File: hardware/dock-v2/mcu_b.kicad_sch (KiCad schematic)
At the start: 31 parts, among them SW401 SW_Push, U401 RP2354A, Y401 12MHz

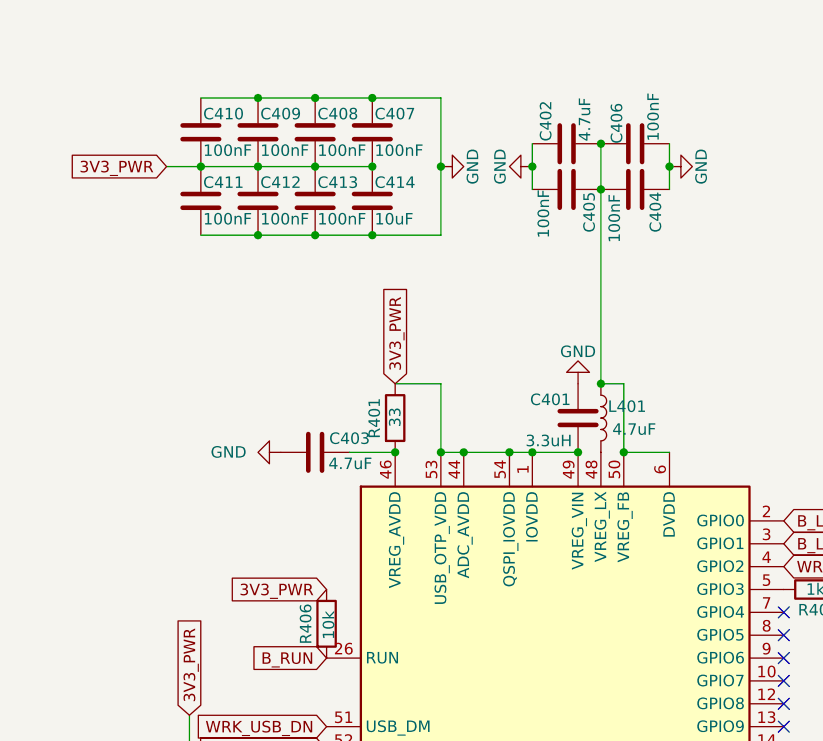
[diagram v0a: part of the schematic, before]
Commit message: Dock v2 schematic: PWR_FLAGs, one name per power net, ESP32 USB test pads dropped
- PWR_FLAGs on GND, VBUS_IN, 5V_PWR, A_1V1, A_VREG_AVDD, B_1V1, B_VREG_AVDD
  (each with a label at a pin of the net, which also names the five nets that
  were unnamed: VBUS_IN, A/B_1V1, A/B_VREG_AVDD)
- GNDPWR symbol -> GND; duplicate +3.3V/+5V power symbols and their now-dangling
  3V3_PWR/5V_PWR labels removed (connectivity verified identical before/after)
- TP501/TP502 (ESP32 GPIO18/19 USB pads) not needed: pins 26/27 are no-connects
  in the model; docs and guides updated (fallback flashing: TXD0/RXD0 pads)

ERC: 0 errors, 0 warnings. check_wiring.py: OK, wiring matches the guide.

Co-Authored-By: Claude Opus 5.5 <noreply@anthropic.com>
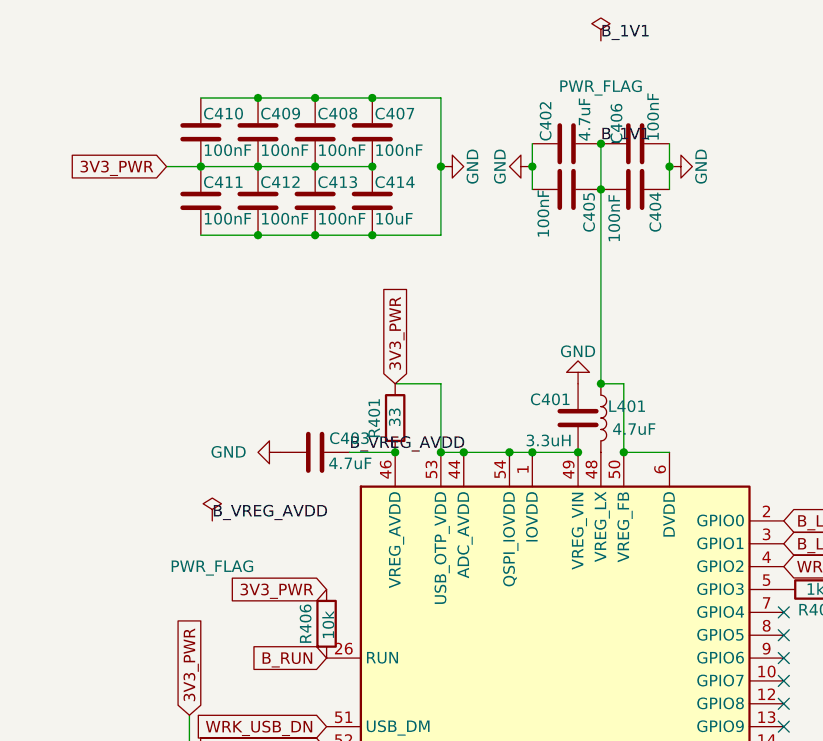
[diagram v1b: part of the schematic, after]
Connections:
- net B_1V1: now reaches C402.2, C404.2, C405.1, C406.1, L401.1, U401.23 (DVDD), U401.39 (DVDD), U401.50 (VREG_FB), U401.6 (DVDD)
- net B_VREG_AVDD: now reaches C403.2, R401.2, U401.46 (VREG_AVDD)
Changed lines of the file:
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@@
+		)
+	)
+	(label "B_1V1"
+		(at 162.56 95.25 0)
+		(fields_autoplaced yes)
+		(effects
+			(font
+				(size 1.27 1.27)
+			)
+			(justify left bottom)
+		)
+	)
+	(symbol
+		(lib_id "power:PWR_FLAG")
+		(at 162.56 83.82 0)
+		(unit 1)
+		(body_style 1)
+		(exclude_from_sim no)
+		(in_bom yes)
+		(on_board yes)
+		(in_pos_files yes)
+		(dnp no)
+		(fields_autoplaced yes)
+		(property "Reference" "#FLG0490"
+			(at 162.56 90.17 0)
+			(hide yes)
+			(show_name no)
+			(do_not_autoplace no)
+			(effects
+				(font
+					(size 1.27 1.27)
+				)
+			)
+		)
+		(property "Value" "PWR_FLAG"
+			(at 162.56 88.9 0)
+			(show_name no)
+			(do_not_autoplace no)
+			(effects
+				(font
+					(size 1.27 1.27)
+				)
+			)
+		)
+		(property "Footprint" ""
+			(at 162.56 83.82 0)
+			(hide yes)
+			(show_name no)
+			(do_not_autoplace no)
+			(effects
+				(font
+					(size 1.27 1.27)
+				)
+			)
+		)
+		(property "Datasheet" ""
+			(at 162.56 83.82 0)
+			(hide yes)
+			(show_name no)
+			(do_not_autoplace no)
+			(effects
+				(font
+					(size 1.27 1.27)
+				)
+			)
+		)
+		(property "Description" "Power symbol creates a global label with name \"GND\" , ground"
+			(at 162.56 83.82 0)
+			(hide yes)
+			(show_name no)
+			(do_not_autoplace no)
+			(effects
+				(font
+					(size 1.27 1.27)
+				)
+			)
+		)
+		(pin "1"
+		)
+		(instances
+			(project "dock-v2"
+				(path "/928a9dc6-b0ce-4f47-a17d-f26fd77e396a/da035690-56be-4ab0-b555-b768c130331c"
+					(reference "#FLG0490")
+					(unit 1)
+				)
+			)
+		)
+	)
+	(label "B_1V1"
+		(at 162.56 83.82 0)
+		(fields_autoplaced yes)
+		(effects
+			(font
+				(size 1.27 1.27)
+			)
+			(justify left bottom)
+		)
+	)
+	(label "B_VREG_AVDD"
+		(at 134.62 129.54 0)
+		(fields_autoplaced yes)
+		(effects
+			(font
+				(size 1.27 1.27)
+			)
+			(justify left bottom)
+		)
+	)
+	(symbol
+		(lib_id "power:PWR_FLAG")
+		(at 119.38 137.16 0)
+		(unit 1)
+		(body_style 1)
+		(exclude_from_sim no)
+		(in_bom yes)
+		(on_board yes)
+		(in_pos_files yes)
+		(dnp no)
+		(fields_autoplaced yes)
+		(property "Reference" "#FLG0491"
+			(at 119.38 143.51 0)
+			(hide yes)
+			(show_name no)
+			(do_not_autoplace no)
+			(effects
+				(font
+					(size 1.27 1.27)
+				)
+			)
+		)
+		(property "Value" "PWR_FLAG"
+			(at 119.38 142.24 0)
+			(show_name no)
+			(do_not_autoplace no)
+			(effects
+				(font
+					(size 1.27 1.27)
+				)
+			)
+		)
+		(property "Footprint" ""
+			(at 119.38 137.16 0)
+			(hide yes)
+			(show_name no)
+			(do_not_autoplace no)
+			(effects
+				(font
+					(size 1.27 1.27)
+				)
+			)
+		)
+		(property "Datasheet" ""
+			(at 119.38 137.16 0)
+			(hide yes)
+			(show_name no)
+			(do_not_autoplace no)
+			(effects
+				(font
+					(size 1.27 1.27)
+				)
+			)
+		)
+		(property "Description" "Power symbol creates a global label with name \"GND\" , ground"
+			(at 119.38 137.16 0)
+			(hide yes)
+			(show_name no)
+			(do_not_autoplace no)
+			(effects
+				(font
+					(size 1.27 1.27)
+				)
+			)
+		)
+		(pin "1"
+		)
+		(instances
+			(project "dock-v2"
+				(path "/928a9dc6-b0ce-4f47-a17d-f26fd77e396a/da035690-56be-4ab0-b555-b768c130331c"
+					(reference "#FLG0491")
+					(unit 1)
+				)
+			)
+		)
+	)
+	(label "B_VREG_AVDD"
+		(at 119.38 137.16 0)
+		(fields_autoplaced yes)
+		(effects
+			(font
+				(size 1.27 1.27)
+			)
+			(justify left bottom)
 		)
 	)
